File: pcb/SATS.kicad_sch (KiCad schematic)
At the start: 15 parts, among them J1 Raspberry_Pi_2_3, J2 A00-432-262-450, J3 AudioJack4_SwitchTR1, SW1 Main Door Switch, SW2 Serv Door Switch, SW3 Third Reed Switch, U1 MCP23017_SP, U2 MCP23017_SP, U3 CD40109BE, U4 IRLZ14PBF

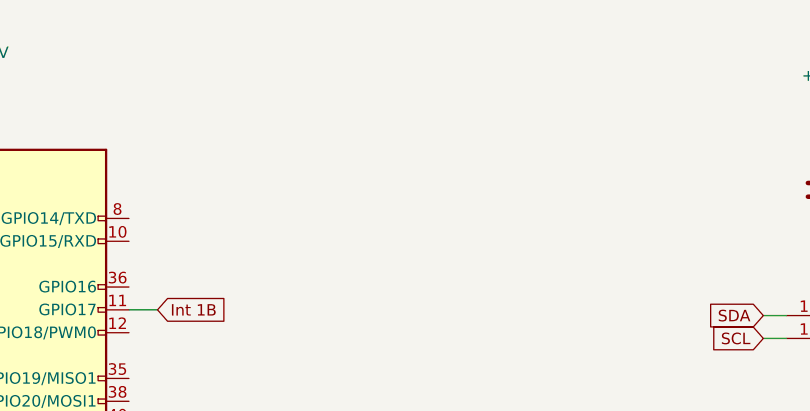
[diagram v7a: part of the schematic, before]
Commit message: Add Power Connectors
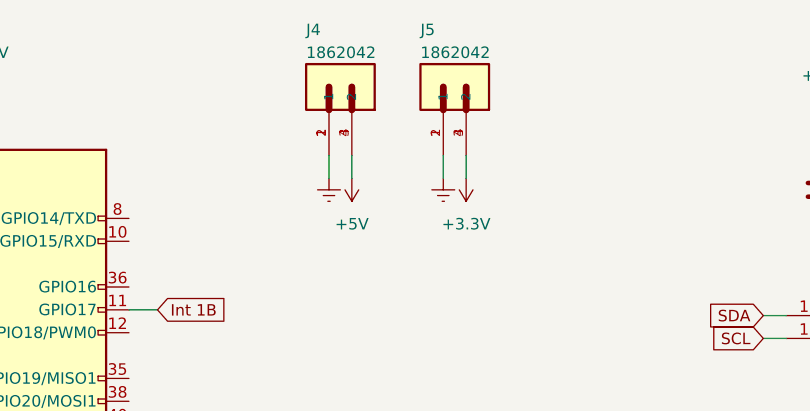
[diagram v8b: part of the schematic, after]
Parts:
- added J4, J5: 1862042, PHOENIX_1862042, symbol TerminalConn:1862042
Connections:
- net +3V3: now also J5.3 (2), J5.4 (2)
- net +5V: now also J4.3 (2), J4.4 (2)
- net Earth: now also J4.1, J4.2 (1), J5.1, J5.2 (1)
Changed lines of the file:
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@@
+    (stroke (width 0) (type default) (color 0 0 0 0))
+  )
+  (wire (pts (xy 106.68 30.48) (xy 106.68 27.94))
     (stroke (width 0) (type default) (color 0 0 0 0))
   )
@@
     (stroke (width 0) (type default) (color 0 0 0 0))
   )
+  (wire (pts (xy 109.22 30.48) (xy 109.22 27.94))
+    (stroke (width 0) (type default) (color 0 0 0 0))
+  )
   (wire (pts (xy 149.225 35.56) (xy 149.225 37.465))
     (stroke (width 0) (type default) (color 0 0 0 0))
@@
     (stroke (width 0) (type default) (color 0 0 0 0))
   )
+  (wire (pts (xy 93.98 30.48) (xy 93.98 27.94))
+    (stroke (width 0) (type default) (color 0 0 0 0))
+  )
   (wire (pts (xy 27.94 34.925) (xy 31.115 34.925))
     (stroke (width 0) (type default) (color 0 0 0 0))
@@
   )
   (wire (pts (xy 31.115 62.865) (xy 27.94 62.865))
+    (stroke (width 0) (type default) (color 0 0 0 0))
+  )
+  (wire (pts (xy 96.52 27.94) (xy 96.52 30.48))
     (stroke (width 0) (type default) (color 0 0 0 0))
   )
@@
     (pin "3")
     (pin "4")
+  )
+  (symbol (lib_id "power:+3.3V") (at 109.22 30.48 0) (mirror x) (unit 1)
+    (in_bom yes) (on_board yes) (fields_autoplaced)
+    (property "Reference" "#PWR?" (id 0) (at 109.22 26.67 0)
+      (effects (font (size 1.27 1.27)) hide)
+    )
+    (property "Value" "+3.3V" (id 1) (at 109.22 35.56 0))
+    (property "Footprint" "" (id 2) (at 109.22 30.48 0)
+      (effects (font (size 1.27 1.27)) hide)
+    )
+    (property "Datasheet" "" (id 3) (at 109.22 30.48 0)
+      (effects (font (size 1.27 1.27)) hide)
+    )
+    (pin "1")
+  )
+  (symbol (lib_id "power:Earth") (at 93.98 30.48 0) (unit 1)
+    (in_bom yes) (on_board yes) (fields_autoplaced)
+    (property "Reference" "#PWR?" (id 0) (at 93.98 36.83 0)
+      (effects (font (size 1.27 1.27)) hide)
+    )
+    (property "Value" "Earth" (id 1) (at 93.98 34.29 0)
+      (effects (font (size 1.27 1.27)) hide)
+    )
+    (property "Footprint" "" (id 2) (at 93.98 30.48 0)
+      (effects (font (size 1.27 1.27)) hide)
+    )
+    (property "Datasheet" "~" (id 3) (at 93.98 30.48 0)
+      (effects (font (size 1.27 1.27)) hide)
+    )
+    (pin "1")
   )
   (symbol (lib_id "power:Earth") (at 201.295 154.94 0) (unit 1)
@@
     (pin "2")
   )
+  (symbol (lib_id "TerminalConn:1862042") (at 93.98 20.32 90) (unit 1)
+    (in_bom yes) (on_board yes)
+    (property "Reference" "J4" (id 0) (at 91.44 13.97 90)
+      (effects (font (size 1.27 1.27)) (justify right))
+    )
+    (property "Value" "1862042" (id 1) (at 91.44 16.51 90)
+      (effects (font (size 1.27 1.27)) (justify right))
+    )
+    (property "Footprint" "PHOENIX_1862042" (id 2) (at 93.98 20.32 0)
+      (effects (font (size 1.27 1.27)) (justify bottom) hide)
+    )
+    (property "Datasheet" "" (id 3) (at 93.98 20.32 0)
+      (effects (font (size 1.27 1.27)) hide)
+    )
+    (property "PARTREV" "01/24/2018" (id 4) (at 93.98 20.32 0)
+      (effects (font (size 1.27 1.27)) (justify bottom) hide)
+    )
+    (property "STANDARD" "Manufacturer recommendations" (id 5) (at 93.98 20.32 0)
+      (effects (font (size 1.27 1.27)) (justify bottom) hide)
+    )
+    (property "MANUFACTURER" "PHOENIX CONTACT" (id 6) (at 93.98 20.32 0)
+      (effects (font (size 1.27 1.27)) (justify bottom) hide)
+    )
+    (pin "1")
+    (pin "2")
+    (pin "3")
+    (pin "4")
+  )
   (symbol (lib_id "power:+5V") (at 92.71 146.685 0) (mirror y) (unit 1)
     (in_bom yes) (on_board yes) (fields_autoplaced)
@@
     )
     (pin "1")
+  )
+  (symbol (lib_id "TerminalConn:1862042") (at 106.68 20.32 90) (unit 1)
+    (in_bom yes) (on_board yes)
+    (property "Reference" "J5" (id 0) (at 104.14 13.97 90)
+      (effects (font (size 1.27 1.27)) (justify right))
+    )
+    (property "Value" "1862042" (id 1) (at 104.14 16.51 90)
+      (effects (font (size 1.27 1.27)) (justify right))
+    )
+    (property "Footprint" "PHOENIX_1862042" (id 2) (at 106.68 20.32 0)
+      (effects (font (size 1.27 1.27)) (justify bottom) hide)
+    )
+    (property "Datasheet" "" (id 3) (at 106.68 20.32 0)
+      (effects (font (size 1.27 1.27)) hide)
+    )
+    (property "PARTREV" "01/24/2018" (id 4) (at 106.68 20.32 0)
+      (effects (font (size 1.27 1.27)) (justify bottom) hide)
+    )
+    (property "STANDARD" "Manufacturer recommendations" (id 5) (at 106.68 20.32 0)
+      (effects (font (size 1.27 1.27)) (justify bottom) hide)
+    )
+    (property "MANUFACTURER" "PHOENIX CONTACT" (id 6) (at 106.68 20.32 0)
+      (effects (font (size 1.27 1.27)) (justify bottom) hide)
+    )
+    (pin "1")
+    (pin "2")
+    (pin "3")
+    (pin "4")
   )
   (symbol (lib_id "power:+3.3V") (at 127 66.675 0) (unit 1)
@@
     (pin "9")
   )
+  (symbol (lib_id "power:+5V") (at 96.52 30.48 0) (mirror x) (unit 1)
+    (in_bom yes) (on_board yes) (fields_autoplaced)
+    (property "Reference" "#PWR?" (id 0) (at 96.52 26.67 0)
+      (effects (font (size 1.27 1.27)) hide)
+    )
+    (property "Value" "+5V" (id 1) (at 96.52 35.56 0))
+    (property "Footprint" "" (id 2) (at 96.52 30.48 0)
+      (effects (font (size 1.27 1.27)) hide)
+    )
+    (property "Datasheet" "" (id 3) (at 96.52 30.48 0)
+      (effects (font (size 1.27 1.27)) hide)
+    )
+    (pin "1")
+  )
   (symbol (lib_id "power:+3.3V") (at 222.25 79.375 0) (unit 1)
     (in_bom yes) (on_board yes)
@@
     (pin "1")
   )
+  (symbol (lib_id "power:Earth") (at 106.68 30.48 0) (unit 1)
+    (in_bom yes) (on_board yes) (fields_autoplaced)
+    (property "Reference" "#PWR?" (id 0) (at 106.68 36.83 0)
+      (effects (font (size 1.27 1.27)) hide)
+    )
+    (property "Value" "Earth" (id 1) (at 106.68 34.29 0)
+      (effects (font (size 1.27 1.27)) hide)
+    )
+    (property "Footprint" "" (id 2) (at 106.68 30.48 0)
+      (effects (font (size 1.27 1.27)) hide)
+    )
+    (property "Datasheet" "~" (id 3) (at 106.68 30.48 0)
+      (effects (font (size 1.27 1.27)) hide)
+    )
+    (pin "1")
+  )
   (symbol (lib_id "power:Earth") (at 242.57 95.885 0) (unit 1)
     (in_bom yes) (on_board yes) (fields_autoplaced)
@@
       (reference "#PWR0133") (unit 1) (value "Earth") (footprint "")
     )
+    (path "/2ac052e5-84c7-4fd1-be06-601f0661c7c7"
+      (reference "#PWR?") (unit 1) (value "+3.3V") (footprint "")
+    )
+    (path "/36b66f18-02ad-4b28-a62e-b77776975e16"
+      (reference "#PWR?") (unit 1) (value "Earth") (footprint "")
+    )
+    (path "/b2fc1d9e-94cf-4a0c-87ad-8ac0a3cf5923"
+      (reference "#PWR?") (unit 1) (value "+5V") (footprint "")
+    )
+    (path "/ccdc7ad5-4b3b-4c5f-9b3c-ca28cd13bffb"
+      (reference "#PWR?") (unit 1) (value "Earth") (footprint "")
+    )
     (path "/76312551-1f93-4c3b-b646-01a8c308431a"
       (reference "C1") (unit 1) (value "100nF") (footprint "Capacitor_THT:C_Rect_L7.0mm_W3.5mm_P5.00mm")
@@
       (reference "J3") (unit 1) (value "AudioJack4_SwitchTR1") (footprint "AudioJack:AudioJack4_6pad")
     )
+    (path "/769ea560-2289-4ed4-9a90-b0dea97e737b"
+      (reference "J4") (unit 1) (value "1862042") (footprint "PHOENIX_1862042")
+    )
+    (path "/9087eb8b-b662-4253-9567-a8b106d45277"
+      (reference "J5") (unit 1) (value "1862042") (footprint "PHOENIX_1862042")
+    )
     (path "/d43a3514-5172-4281-8334-eb9c6c36fa38"
